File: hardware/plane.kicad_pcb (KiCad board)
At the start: 2 copper layers, 32 x 100 mm, 46 parts, among them J1 USB_B_Micro, J2 Conn_Coaxial, J3 Conn_01x03, J4 Conn_01x03, J5 Conn_01x03, J6 Conn_01x03, J7 Conn_01x02, Q1 BSS138, Q2 BSS138, U1 ESP32-WROOM-32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

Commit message: upgrade esc connector & sma
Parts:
- removed BATT, GND, PWM: TestPoint, TestPoint:TestPoint_Pad_2.5x2.5mm
- added C18: C, Capacitor_SMD:C_0603_1608Metric, F.Cu at (105.5, 47.8)
- added J8: Conn_01x03, Connector_PinHeader_2.54mm:PinHeader_1x03_P2.54mm_Vertical, F.Cu at (102.8, 46.0)
- added TP2: TestPoint, TestPoint:TestPoint_Pad_2.5x2.5mm, F.Cu at (102.8, 58.2)
- added TP3: TestPoint, TestPoint:TestPoint_Pad_2.5x2.5mm, F.Cu at (102.8, 54.8)
- J2: footprint Connector_Coaxial:SMA_Amphenol_132289_EdgeMount -> Connector_Coaxial:SMA_Samtec_SMA-J-P-H-ST-EM1_EdgeMount
- moved J2 0.84 mm to (116.0, 137.8)
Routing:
- net MOTOR: track 4.98 -> 11.2 mm, vias 0 -> 1
- net +5V: track 149.0 -> 152.7 mm
- net +BATT: track 57.6 -> 54.2 mm
- net SS: track 96.6 -> 95.8 mm
- net GND: vias 66 -> 75

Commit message: rewire
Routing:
- net +5V: track 152.7 -> 189.1 mm, vias 27 -> 29
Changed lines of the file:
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@@
 	)
 	(via
-		(at 105.25 50)
+		(at 104.2 49.8)
 		(size 0.8)
 		(drill 0.6)
@@
 	)
 	(segment
+		(start 110.6 86.25)
+		(end 110.5 86.35)
+		(width 0.5)
+		(layer "F.Cu")
+		(net 3)
+	)
+	(segment
 		(start 105.775 118.5)
 		(end 105.775 120.5)
+		(width 0.5)
+		(layer "F.Cu")
+		(net 3)
+	)
+	(segment
+		(start 105.875 78.641942)
+		(end 105.875 83.1)
 		(width 0.5)
 		(layer "F.Cu")
@@
 	)
 	(segment
-		(start 109 86.25)
-		(end 114 86.25)
-		(width 0.5)
-		(layer "F.Cu")
-		(net 3)
-	)
-	(segment
 		(start 126.125 83.375)
 		(end 126.5 83)
@@
 	)
 	(segment
+		(start 105.875 83.1)
+		(end 106 83.225)
+		(width 0.5)
+		(layer "F.Cu")
+		(net 3)
+	)
+	(segment
+		(start 110.5 100.25)
+		(end 110.5 86.35)
+		(width 0.5)
+		(layer "F.Cu")
+		(net 3)
+	)
+	(segment
 		(start 108.2 113.85)
 		(end 108.2 112.45)
@@
 	)
 	(segment
+		(start 105.5 49.7)
+		(end 105.5 48.525)
+		(width 0.2)
+		(layer "F.Cu")
+		(net 3)
+	)
+	(segment
 		(start 108.75 136.25)
 		(end 106.235 136.25)
@@
 	)
 	(segment
-		(start 110.5 100.25)
-		(end 110.5 87.75)
-		(width 0.5)
-		(layer "F.Cu")
-		(net 3)
-	)
-	(segment
 		(start 105.775 124.725)
 		(end 105.775 120.5)
@@
 		(start 103.775 135)
 		(end 103.775 137.29)
-		(width 0.5)
-		(layer "F.Cu")
-		(net 3)
-	)
-	(segment
-		(start 110.5 87.75)
-		(end 109 86.25)
-		(width 0.5)
-		(layer "F.Cu")
-		(net 3)
-	)
-	(segment
-		(start 106 83.25)
-		(end 109 86.25)
 		(width 0.5)
 		(layer "F.Cu")
@@
 	)
 	(segment
+		(start 114 86.25)
+		(end 110.6 86.25)
+		(width 0.5)
+		(layer "F.Cu")
+		(net 3)
+	)
+	(segment
+		(start 106 83.225)
+		(end 107.2 83.225)
+		(width 0.5)
+		(layer "F.Cu")
+		(net 3)
+	)
+	(segment
 		(start 105.780912 115.219088)
 		(end 107.15 113.85)
@@
 	)
 	(segment
-		(start 106 83.225)
-		(end 106 83.25)
-		(width 0.5)
-		(layer "F.Cu")
-		(net 3)
-	)
-	(segment
 		(start 106.235 136.25)
 		(end 104.485 138)
@@
 	)
 	(segment
+		(start 107.2 83.225)
+		(end 107.425 83.225)
+		(width 0.5)
+		(layer "F.Cu")
+		(net 3)
+	)
+	(segment
 		(start 114.75 100.25)
 		(end 110.5 100.25)
@@
 		(net 3)
 	)
+	(segment
+		(start 107.425 83.225)
+		(end 110.5 86.3)
+		(width 0.5)
+		(layer "F.Cu")
+		(net 3)
+	)
+	(segment
+		(start 105.6 49.8)
+		(end 105.5 49.7)
+		(width 0.2)
+		(layer "F.Cu")
+		(net 3)
+	)
+	(segment
+		(start 110.5 86.3)
+		(end 110.5 86.35)
+		(width 0.5)
+		(layer "F.Cu")
+		(net 3)
+	)
 	(via
 		(at 112.5 107)
@@
 	)
 	(via
+		(at 105.6 49.8)
+		(size 0.6)
+		(drill 0.3)
+		(layers "F.Cu" "B.Cu")
+		(net 3)
+	)
+	(via
 		(at 107 110.5)
 		(size 0.8)
@@
 		(layers "F.Cu" "B.Cu")
 		(free yes)
+		(net 3)
+	)
+	(via
+		(at 105.875 78.641942)
+		(size 0.6)
+		(drill 0.3)
+		(layers "F.Cu" "B.Cu")
 		(net 3)
 	)
@@
 	)
 	(segment
+		(start 105.875 78.641942)
+		(end 106.475 78.041942)
+		(width 0.5)
+		(layer "B.Cu")
+		(net 3)
+	)
+	(segment
+		(start 106.769239 49.55)
+		(end 105.85 49.55)
+		(width 0.5)
+		(layer "B.Cu")
+		(net 3)
+	)
+	(segment
+		(start 106.475 78.041942)
+		(end 106.475 51.144239)
+		(width 0.5)
+		(layer "B.Cu")
+		(net 3)
+	)
+	(segment
 		(start 108.75 134.75)
 		(end 119.75 123.75)
@@
 	)
 	(segment
+		(start 106.475 51.144239)
+		(end 107.2 50.419239)
+		(width 0.5)
+		(layer "B.Cu")
+		(net 3)
+	)
+	(segment
+		(start 107.2 49.980761)
+		(end 106.769239 49.55)
+		(width 0.5)
+		(layer "B.Cu")
+		(net 3)
+	)
+	(segment
+		(start 107.2 50.419239)
+		(end 107.2 49.980761)
+		(width 0.5)
+		(layer "B.Cu")
+		(net 3)
+	)
+	(segment
 		(start 115.75 84.5)
 		(end 114 86.25)
@@
 		(width 0.5)
 		(layer "B.Cu")
+		(net 3)
+	)
+	(segment
+		(start 105.85 49.55)
+		(end 105.6 49.8)
+		(width 0.5)
+		(layer "B.Cu")

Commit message: add servo connector
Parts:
- added C19: C, Capacitor_SMD:C_0603_1608Metric, F.Cu at (126.5, 93.0)
- added J9: Conn_01x03, Connector_PinHeader_2.54mm:PinHeader_1x03_P2.54mm_Vertical, F.Cu at (129.3, 89.7)
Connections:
- U1 pad 24: unconnected-(U1-IO2-Pad24) -> SR5
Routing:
- net SR5: track 0.00 -> 40.0 mm, vias 0 -> 2
- net +5V: track 189.1 -> 202.2 mm
- net GND: vias 75 -> 86

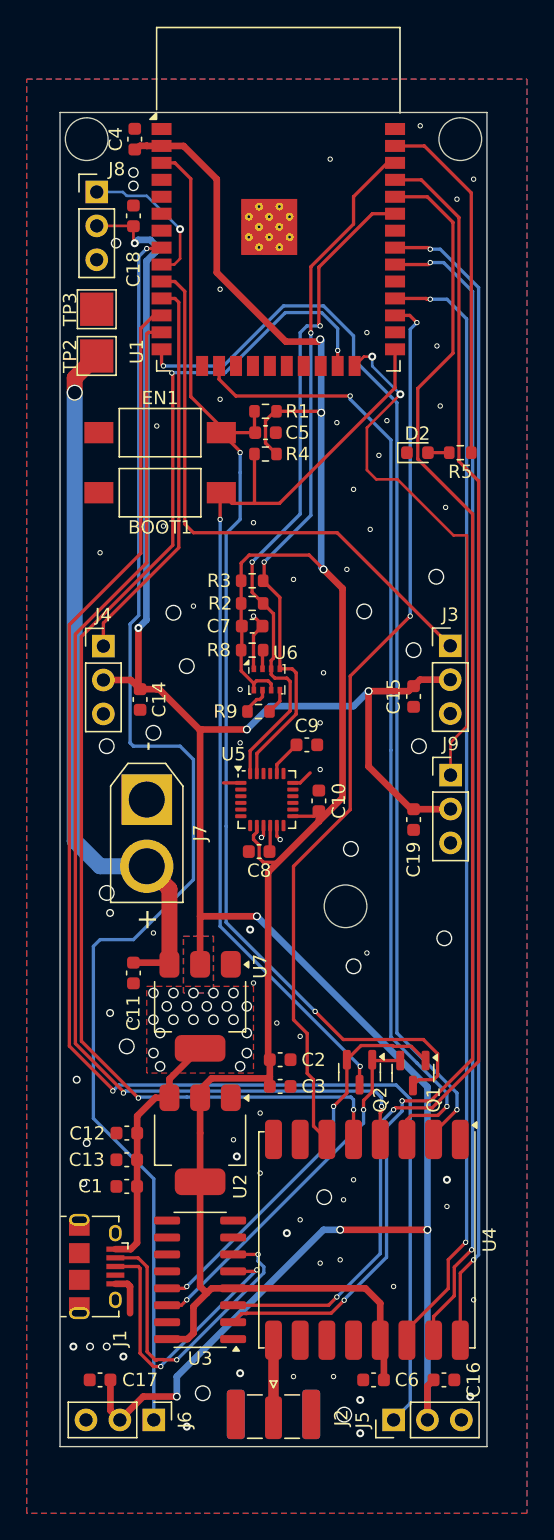
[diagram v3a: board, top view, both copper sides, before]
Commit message: add i2c and uart connectors
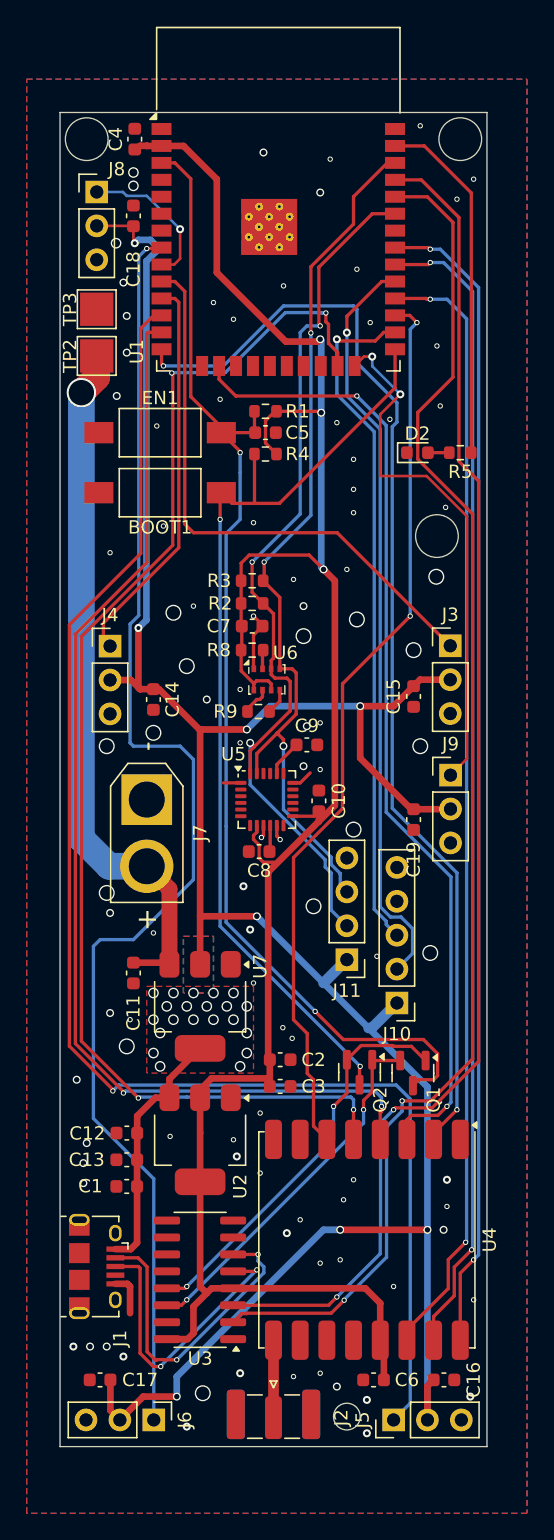
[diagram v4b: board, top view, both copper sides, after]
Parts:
- added J10: Conn_01x05_Pin, Connector_PinHeader_2.54mm:PinHeader_1x05_P2.54mm_Vertical, F.Cu at (125.2, 106.8)
- added J11: Conn_01x04_Pin, Connector_PinHeader_2.54mm:PinHeader_1x04_P2.54mm_Vertical, F.Cu at (121.5, 103.5)
- moved C14 1.00 mm to (107.0, 84.0)
- moved J4 0.50 mm to (103.8, 80.0)
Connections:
- U1 pad 26: unconnected-(U1-IO4-Pad26) -> UART_TX
- U1 pad 29: unconnected-(U1-IO5-Pad29) -> UART_RX
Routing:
- net UART_RX: track 0.00 -> 56.6 mm, vias 0 -> 1
- net UART_TX: track 0.00 -> 51.2 mm, vias 0 -> 1
- net SDA: track 51.2 -> 68.3 mm, vias 2 -> 3
- net SCL: track 53.0 -> 67.1 mm, vias 2 -> 3
- net +5V: track 202.2 -> 206.7 mm
- net MISO: track 82.5 -> 84.1 mm
- net +BATT: track 54.2 -> 53.4 mm
- net MOSI: track 72.5 -> 73.0 mm
- net GND: vias 86 -> 102
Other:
- outline, holes or cut-outs redrawn
